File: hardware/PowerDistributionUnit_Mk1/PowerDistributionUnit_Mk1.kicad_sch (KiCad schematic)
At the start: 0 parts

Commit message: initial schematic
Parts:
- added F1, F2, F3, F4: 3568, Fuse:Fuseholder_Blade_Mini_Keystone_3568, symbol PowerDistributionUnitLib:3568
- added H1, H2, H3, H4, H5, H6: MountingHole_Pad, MountingHole:MountingHole_3.2mm_M3_Pad, symbol Mechanical:MountingHole_Pad
- added J1: XT-30, UTSVT_Connectors:AMASS_XT30UPB-M_1x02_P5.0mm_Vertical, symbol PowerDistributionUnitLib:AMASS_XT-30_Vertical
- added J2: Molex_NanoFit_2x8, PowerDistributionUnitLib:CONN_SD-105312-100_16_MOL, symbol PowerDistributionUnitLib:Molex_NanoFit_2x8_Alt
- added J3: Molex_NanoFit_1x4, PowerDistributionUnitLib:CONN_SD-105309-100_04_MOL, symbol PowerDistributionUnitLib:Molex_NanoFit_1x4
- added J4, J5, J6, J7, J8, J9: Molex_NanoFit_1x2, PowerDistributionUnitLib:CONN_SD-105309-100_02_MOL, symbol PowerDistributionUnitLib:Molex_NanoFit_1x2
- added TP1, TP10, TP11, TP12, TP13, TP14, TP15, TP16, TP191, TP192, TP193, TP194, TP6, TP7, TP8, TP9: TestPoint, Connector_PinHeader_2.54mm:PinHeader_1x01_P2.54mm_Vertical, symbol Connector:TestPoint
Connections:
- new net: F3.2, J6.1 (Pin_1), TP193.1
- new net: F4.2, J7.1 (Pin_1), TP194.1
- new net: F1.2, J4.1 (Pin_1), TP191.1
- new net: F2.2, J5.1 (Pin_1), TP192.1
- new net +3.3V: TP6.1
- new net +3.3VA: TP7.1
- new net CAN_H: J8.1 (Pin_1), J9.1 (Pin_1)
- new net CAN_L: J8.2 (Pin_2), J9.2 (Pin_2)
- new net GND: H1.1, H2.1, H3.1, H4.1, H5.1, H6.1, TP10.1, TP11.1, TP12.1, TP13.1, TP14.1, TP15.1, TP8.1, TP9.1
- new net GNDA: TP16.1
- new net GNDPWR: J1.1 (Pin_1), J3.1 (Pin_1), J3.2 (Pin_2), J3.3 (Pin_3), J3.4 (Pin_4), J4.2 (Pin_2), J5.2 (Pin_2), J6.2 (Pin_2), J7.2 (Pin_2)
- new net InputProtection/LV_IN: J1.2 (Pin_2), TP1.1
- new net LV_OUT.0: F1.1, J2.1 (Pin_1)
- new net LV_OUT.1: F2.1, J2.2 (Pin_2)
- new net LV_OUT.10: J2.11 (Pin_11)
- new net LV_OUT.11: J2.12 (Pin_12)
- new net LV_OUT.12: J2.13 (Pin_13)
- new net LV_OUT.13: J2.14 (Pin_14)
- new net LV_OUT.14: J2.15 (Pin_15)
- new net LV_OUT.15: J2.16 (Pin_16)
- new net LV_OUT.2: F3.1, J2.3 (Pin_3)
- new net LV_OUT.3: F4.1, J2.4 (Pin_4)
- new net LV_OUT.4: J2.5 (Pin_5)
- new net LV_OUT.5: J2.6 (Pin_6)
- new net LV_OUT.6: J2.7 (Pin_7)
- new net LV_OUT.7: J2.8 (Pin_8)
- new net LV_OUT.8: J2.9 (Pin_9)
- new net LV_OUT.9: J2.10 (Pin_10)
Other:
- added sheet Indicators (Indicators.kicad_sch)
- added sheet InputProtection (InputProtection.kicad_sch)
- added sheet LeaderSOM (LeaderSOM.kicad_sch)
- added sheet Monitoring (Monitoring.kicad_sch)
- added sheet Outputs (Outputs.kicad_sch)
- note added: "External Outputs (to PDUBB)"
- note added: "Internal Outputs (intra-enclosure connections)"
- company: (none) -> Longhorn Racing Solar
- title: (none) -> Big Brain Power Distribution Unit (Mk.1)

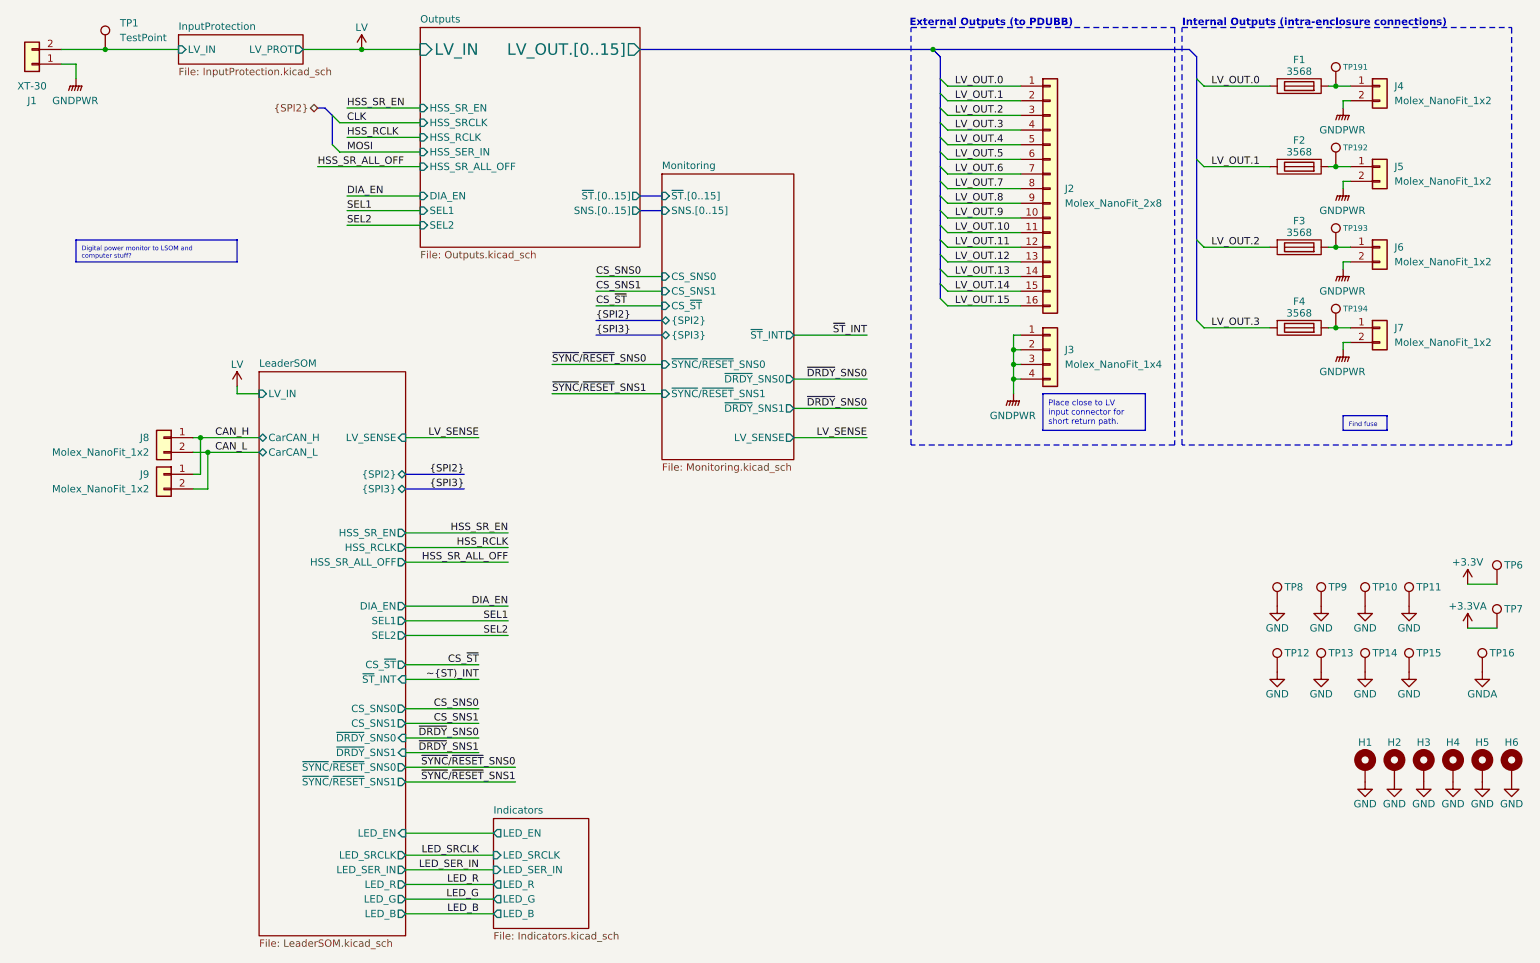
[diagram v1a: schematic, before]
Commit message: schematic updates (found switch, LED resistor values, LV sense ADC pin filter, removed unnecessary parallel resistors, switched to new SR), addressed review comments (input fuse, 3.3V LED, SPI naming fix)
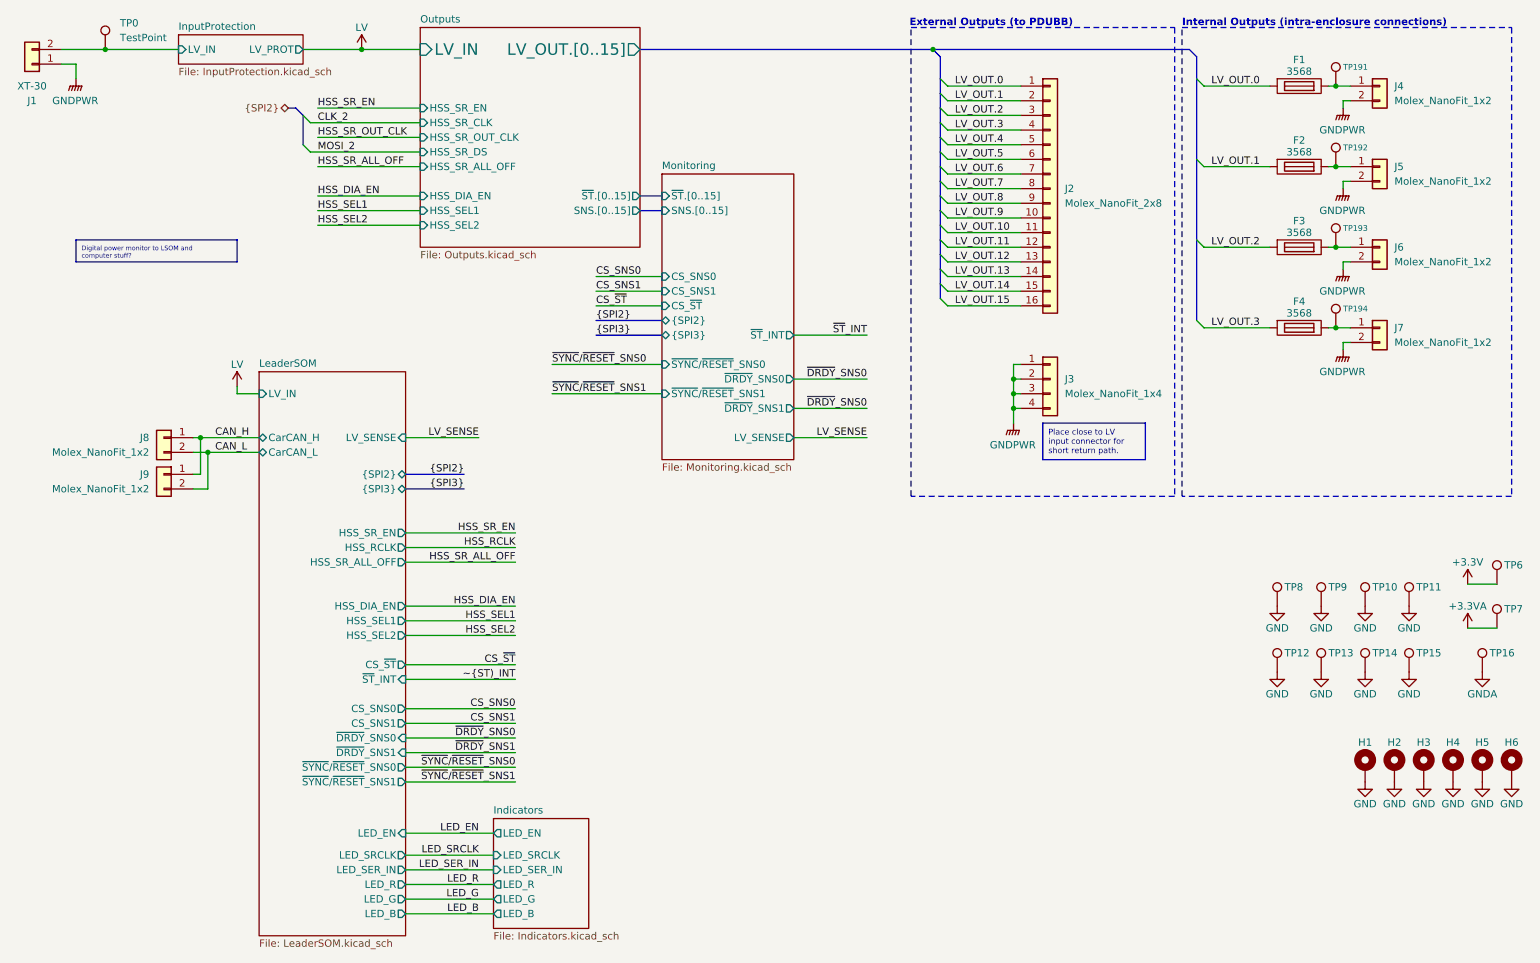
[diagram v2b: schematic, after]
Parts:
- renumbered TP1 to TP0
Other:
- sheet LeaderSOM ports: added HSS_DIA_EN, HSS_SEL1, HSS_SEL2; removed DIA_EN, SEL1, SEL2
- sheet Outputs ports: added HSS_DIA_EN, HSS_SEL1, HSS_SEL2, HSS_SR_CLK, HSS_SR_DS, HSS_SR_OUT_CLK; removed DIA_EN, HSS_RCLK, HSS_SER_IN, HSS_SRCLK, SEL1, SEL2
- moved on the sheet: J3

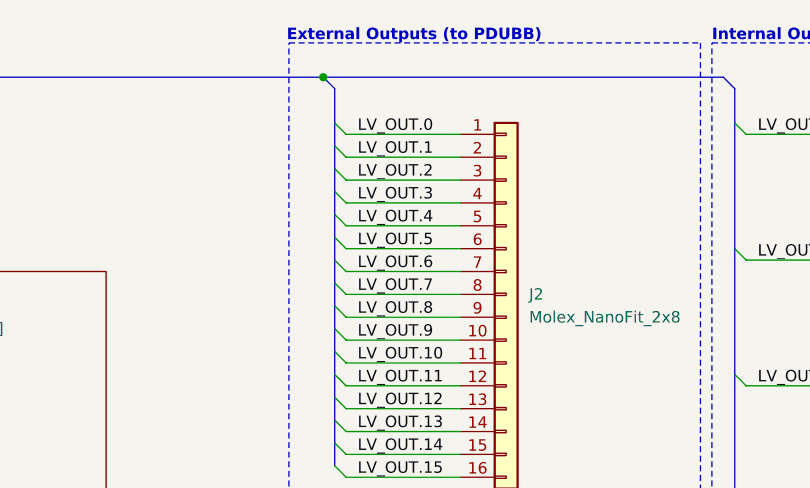
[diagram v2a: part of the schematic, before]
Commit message: change pinout on output connector, output traces attempt 1
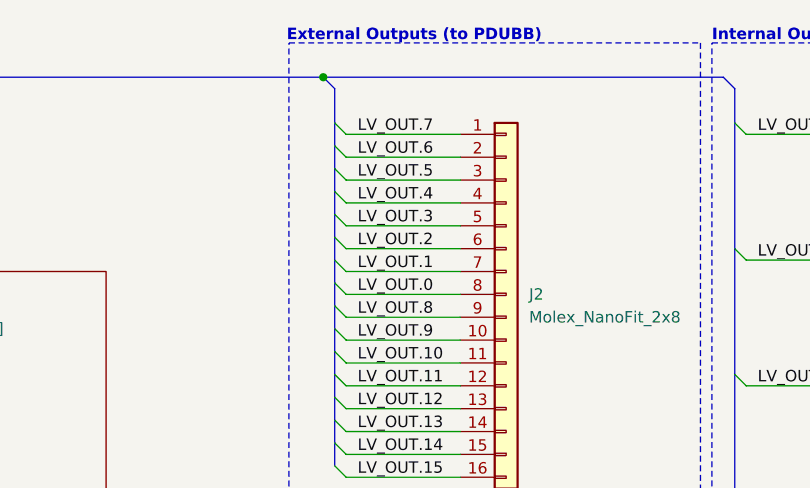
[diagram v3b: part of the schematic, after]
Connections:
- net LV_OUT.0: now also J2.8 (Pin_8); no longer J2.1 (Pin_1)
- net LV_OUT.1: now also J2.7 (Pin_7); no longer J2.2 (Pin_2)
- net LV_OUT.2: now also J2.6 (Pin_6); no longer J2.3 (Pin_3)
- net LV_OUT.3: now also J2.5 (Pin_5); no longer J2.4 (Pin_4)
- net LV_OUT.4: now also J2.4 (Pin_4); no longer J2.5 (Pin_5)
- net LV_OUT.5: now also J2.3 (Pin_3); no longer J2.6 (Pin_6)
- net LV_OUT.6: now also J2.2 (Pin_2); no longer J2.7 (Pin_7)
- net LV_OUT.7: now also J2.1 (Pin_1); no longer J2.8 (Pin_8)
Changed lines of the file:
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@@
 	)
 	(label "LV_OUT.4"
-		(at 180.34 45.72 0)
+		(at 180.34 43.18 0)
 		(effects
 			(font
@@
 	)
 	(label "LV_OUT.6"
-		(at 180.34 50.8 0)
+		(at 180.34 38.1 0)
 		(effects
 			(font
@@
 	)
 	(label "LV_OUT.5"
-		(at 180.34 48.26 0)
+		(at 180.34 40.64 0)
 		(effects
 			(font
@@
 	)
 	(label "LV_OUT.0"
-		(at 180.34 35.56 0)
+		(at 180.34 53.34 0)
 		(effects
 			(font
@@
 	)
 	(label "LV_OUT.2"
-		(at 180.34 40.64 0)
+		(at 180.34 48.26 0)
 		(effects
 			(font
@@
 	)
 	(label "LV_OUT.1"
-		(at 180.34 38.1 0)
+		(at 180.34 50.8 0)
 		(effects
 			(font
@@
 	)
 	(label "LV_OUT.3"
-		(at 180.34 43.18 0)
+		(at 180.34 45.72 0)
 		(effects
 			(font
@@
 	)
 	(label "LV_OUT.7"
-		(at 180.34 53.34 0)
-		(effects
-			(font
+		(at 180.34 35.56 0)
+		(effects
+			(font

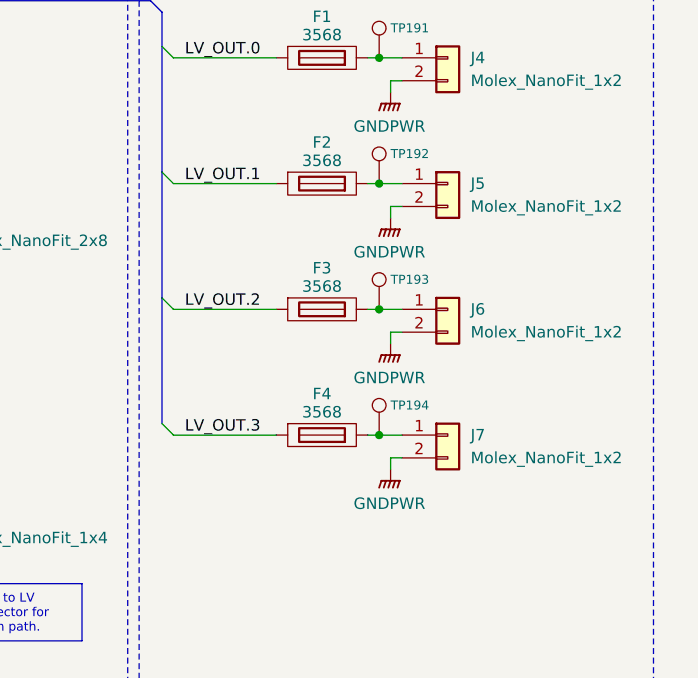
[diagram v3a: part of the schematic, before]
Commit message: add internal output connectors (reduced to 2)
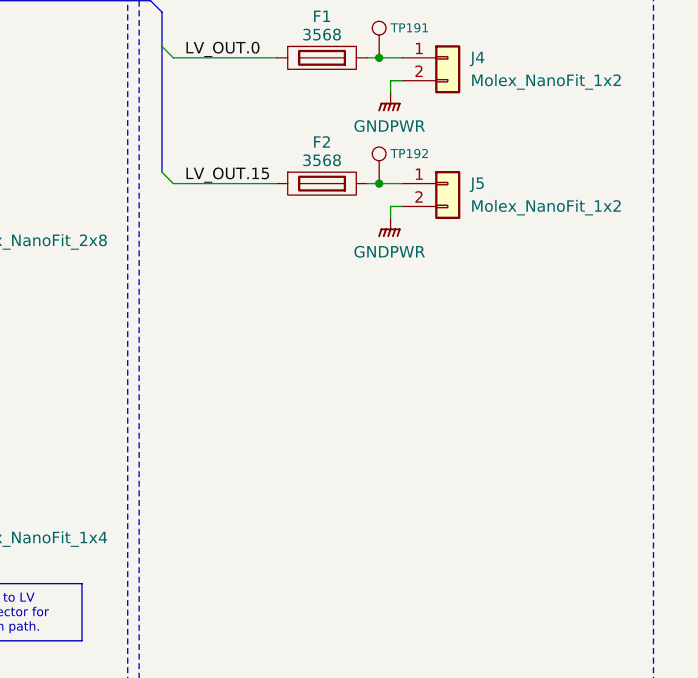
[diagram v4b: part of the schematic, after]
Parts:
- removed F3, F4: 3568, Fuse:Fuseholder_Blade_Mini_Keystone_3568, symbol PowerDistributionUnitLib:3568
- removed J6, J7: Molex_NanoFit_1x2, PowerDistributionUnitLib:CONN_SD-105309-100_02_MOL, symbol PowerDistributionUnitLib:Molex_NanoFit_1x2
- removed TP193, TP194: TestPoint, Connector_PinHeader_2.54mm:PinHeader_1x01_P2.54mm_Vertical, symbol Connector:TestPoint
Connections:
- net LV_OUT.1: no longer F2.1
- net LV_OUT.15: now also F2.1
